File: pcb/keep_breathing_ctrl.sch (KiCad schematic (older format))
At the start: 5 parts, among them P1 CONN_RASPBERRY

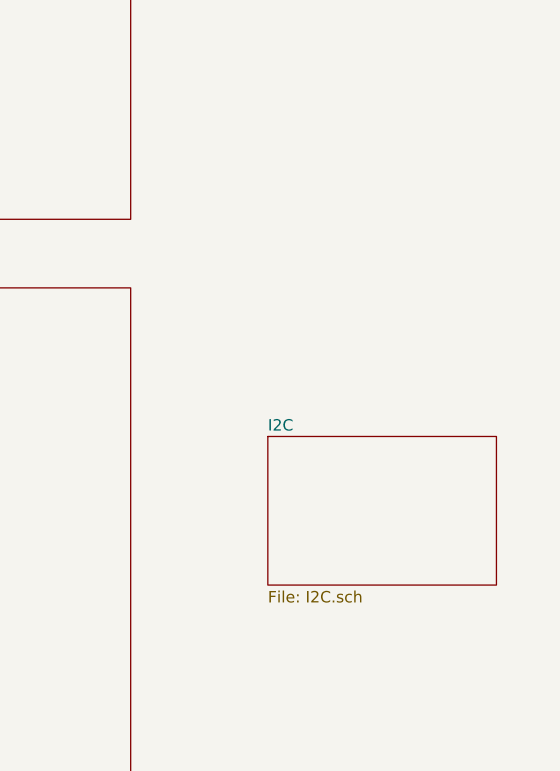
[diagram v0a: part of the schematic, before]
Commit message: RTC to PCB
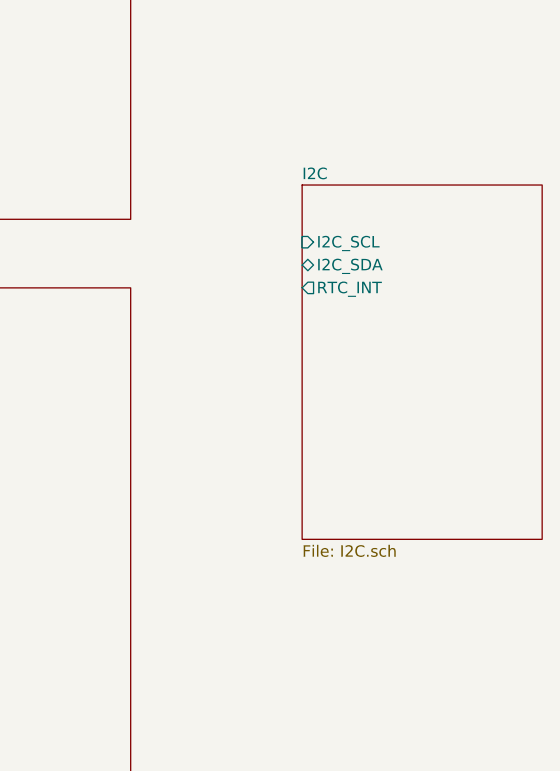
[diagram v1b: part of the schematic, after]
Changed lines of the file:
@@
 $EndSheet
 $Sheet
-S 8550 3150 1000 650
+S 8700 2050 1050 1550
 U 5E8F4152
 F0 "I2C" 50
 F1 "I2C.sch" 50
+F2 "I2C_SDA" B L 8700 2400 50
+F3 "I2C_SCL" I L 8700 2300 50
+F4 "RTC_INT" O L 8700 2500 50
 $EndSheet
 $EndSCHEMATC

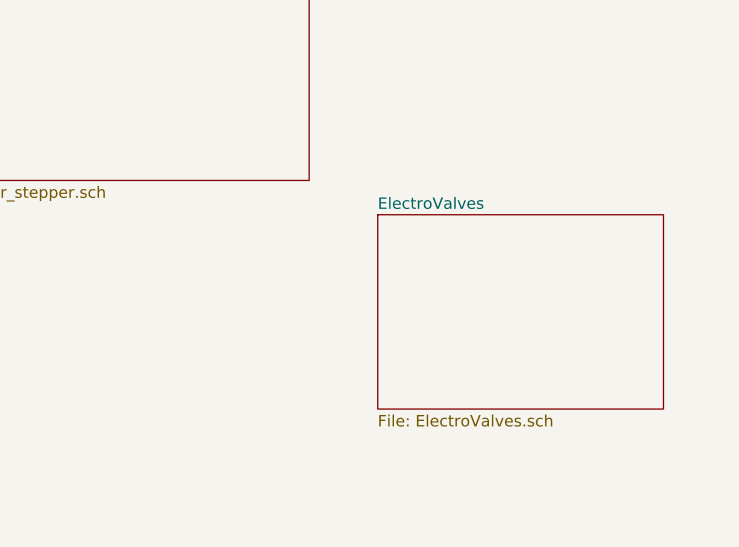
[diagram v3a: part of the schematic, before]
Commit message: connecting relays to the i2c-gpios
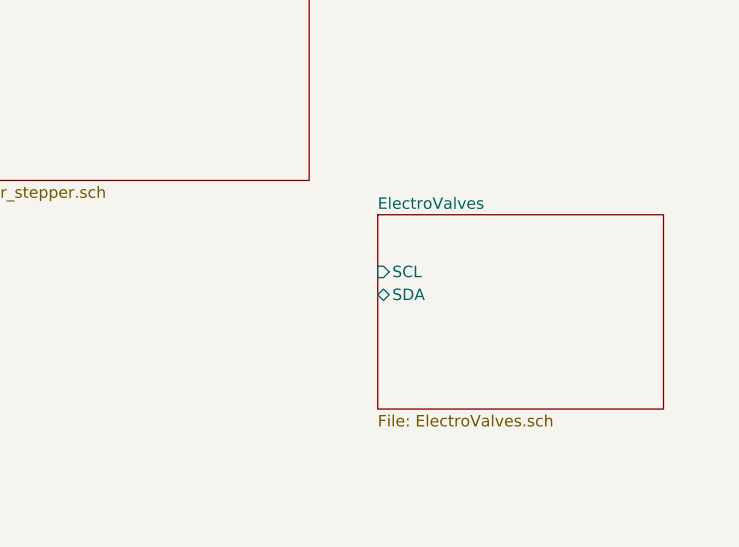
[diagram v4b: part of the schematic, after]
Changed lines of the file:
@@
 F0 "ElectroValves" 50
 F1 "ElectroValves.sch" 50
+F2 "SCL" I L 8250 5250 50
+F3 "SDA" B L 8250 5350 50
 $EndSheet
 $Comp

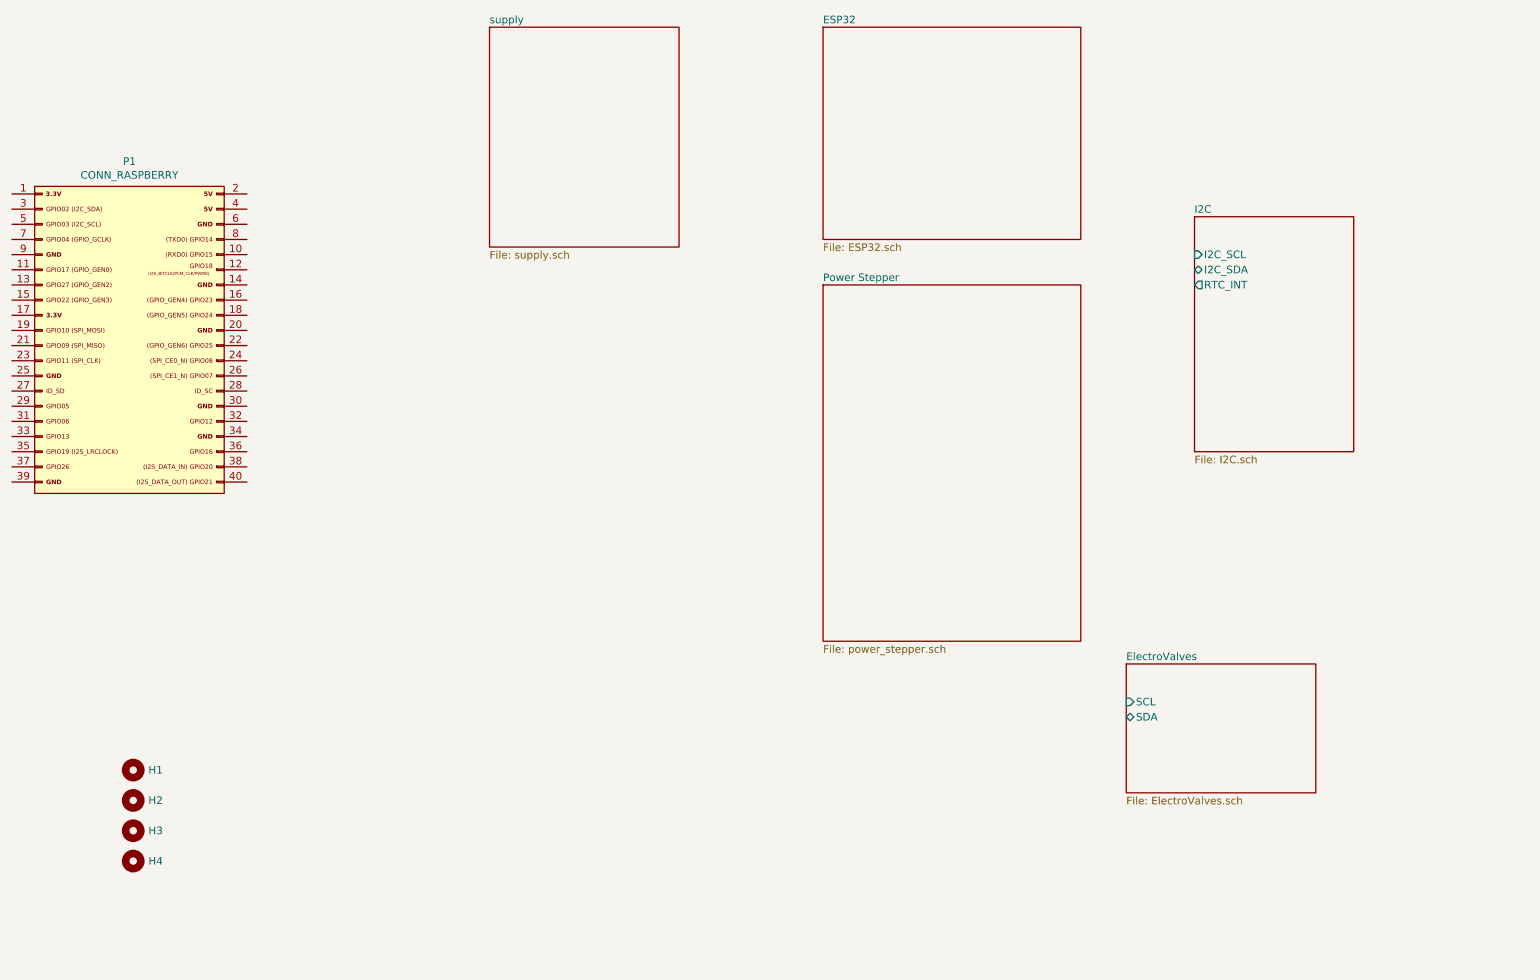
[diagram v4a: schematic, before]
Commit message: connecting esp32 signals
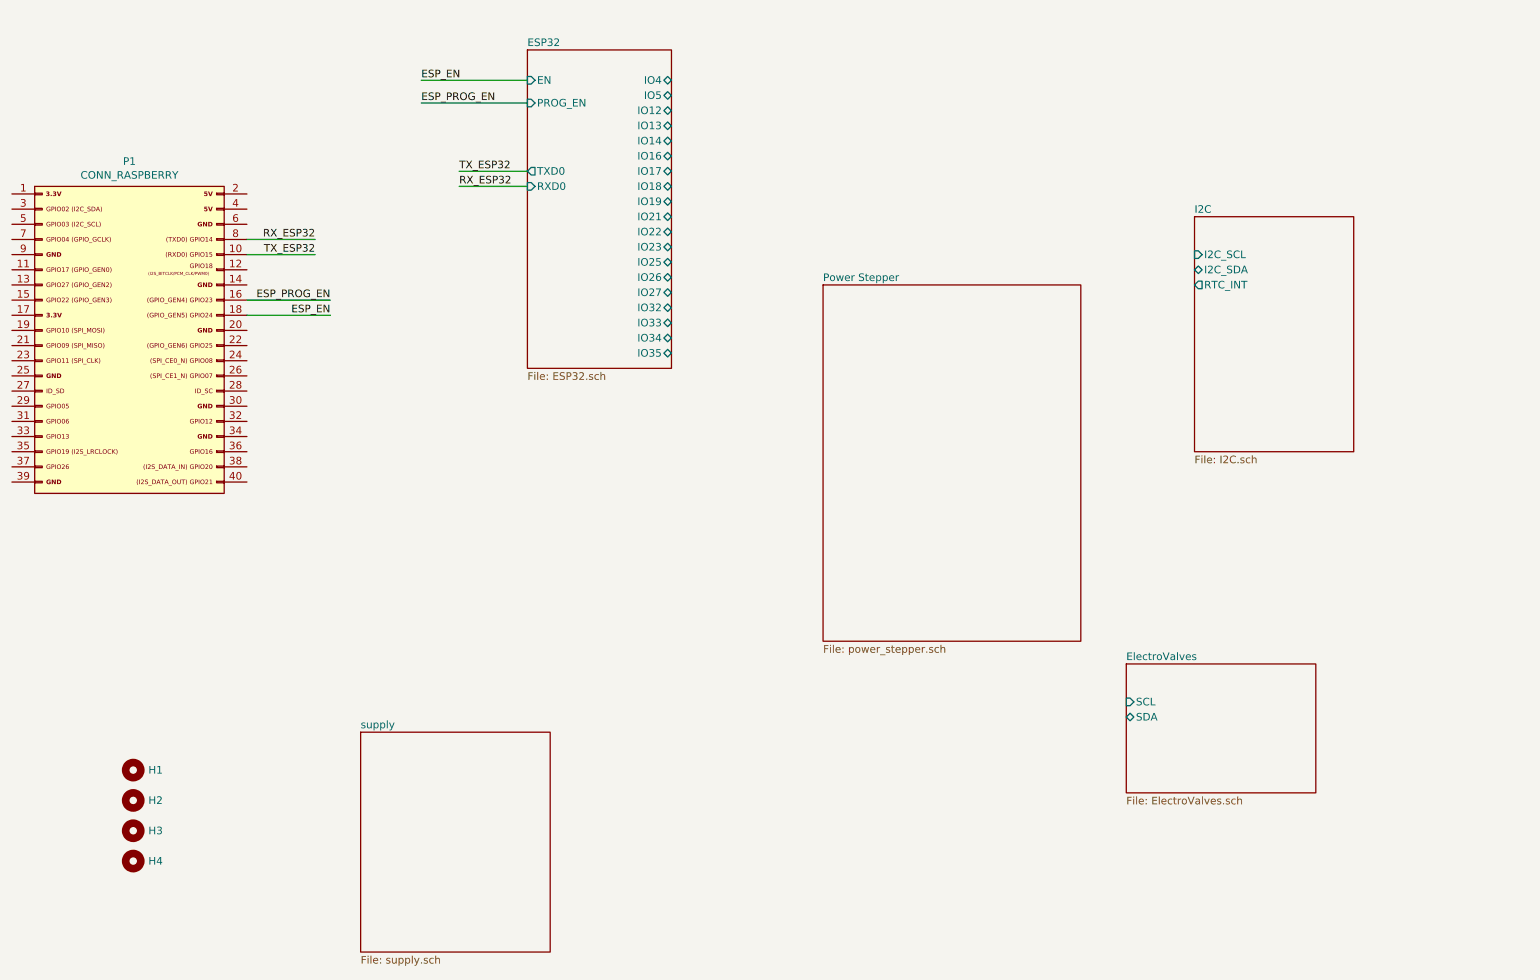
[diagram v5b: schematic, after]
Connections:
- net TX_ESP32: now reaches P1.10 (P10)
- net ESP_PROG_EN: now reaches P1.16 (P16)
- net ESP_EN: now reaches P1.18 (P18)
- net RX_ESP32: now reaches P1.8 (P8)
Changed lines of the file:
@@
 $EndComp
 $Sheet
-S 6250 800  1700 1400
+S 4300 950  950  2100
 U 5E9877D5
 F0 "ESP32" 50
 F1 "ESP32.sch" 50
+F2 "TXD0" O L 4300 1750 50
+F3 "RXD0" I L 4300 1850 50
+F4 "PROG_EN" I L 4300 1300 50
+F5 "IO23" B R 5250 2250 50
+F6 "IO22" B R 5250 2150 50
+F7 "IO19" B R 5250 1950 50
+F8 "IO18" B R 5250 1850 50
+F9 "IO5" B R 5250 1250 50
+F10 "IO17" B R 5250 1750 50
+F11 "IO16" B R 5250 1650 50
+F12 "IO4" B R 5250 1150 50
+F13 "IO12" B R 5250 1350 50
+F14 "IO14" B R 5250 1550 50
+F15 "IO27" B R 5250 2550 50
+F16 "IO26" B R 5250 2450 50
+F17 "IO25" B R 5250 2350 50
+F18 "IO33" B R 5250 2750 50
+F19 "IO32" B R 5250 2650 50
+F20 "IO35" B R 5250 2950 50
+F21 "IO34" B R 5250 2850 50
+F22 "IO13" B R 5250 1450 50
+F23 "IO21" B R 5250 2050 50
+F24 "EN" I L 4300 1150 50
 $EndSheet
 $Sheet
@@
 $EndComp
 $Sheet
-S 4050 800  1250 1450
+S 3200 5450 1250 1450
 U 5E8E60A3
 F0 "supply" 50
@@
 F4 "RTC_INT" O L 8700 2500 50
 $EndSheet
+Wire Wire Line
+	4300 1750 3850 1750
+Wire Wire Line
+	3850 1850 4300 1850
+Text Label 3850 1750 0    50   ~ 0
+TX_ESP32
+Text Label 3850 1850 0    50   ~ 0
+RX_ESP32
+Wire Wire Line
+	2450 2300 2900 2300
+Wire Wire Line
+	2900 2200 2450 2200
+Text Label 2900 2300 2    50   ~ 0
+TX_ESP32
+Text Label 2900 2200 2    50   ~ 0
+RX_ESP32
+Text Label 3600 1300 0    50   ~ 0
+ESP_PROG_EN
+Wire Wire Line
+	4300 1150 3600 1150
+Wire Wire Line
+	4300 1300 3600 1300
+Text Label 3600 1150 0    50   ~ 0
+ESP_EN
+Text Label 3000 2600 2    50   ~ 0
+ESP_PROG_EN
+Wire Wire Line
+	2450 2700 3000 2700
+Wire Wire Line
+	2450 2600 3000 2600
+Text Label 3000 2700 2    50   ~ 0
+ESP_EN
 $EndSCHEMATC

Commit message: added connections to ElectroValves sheet
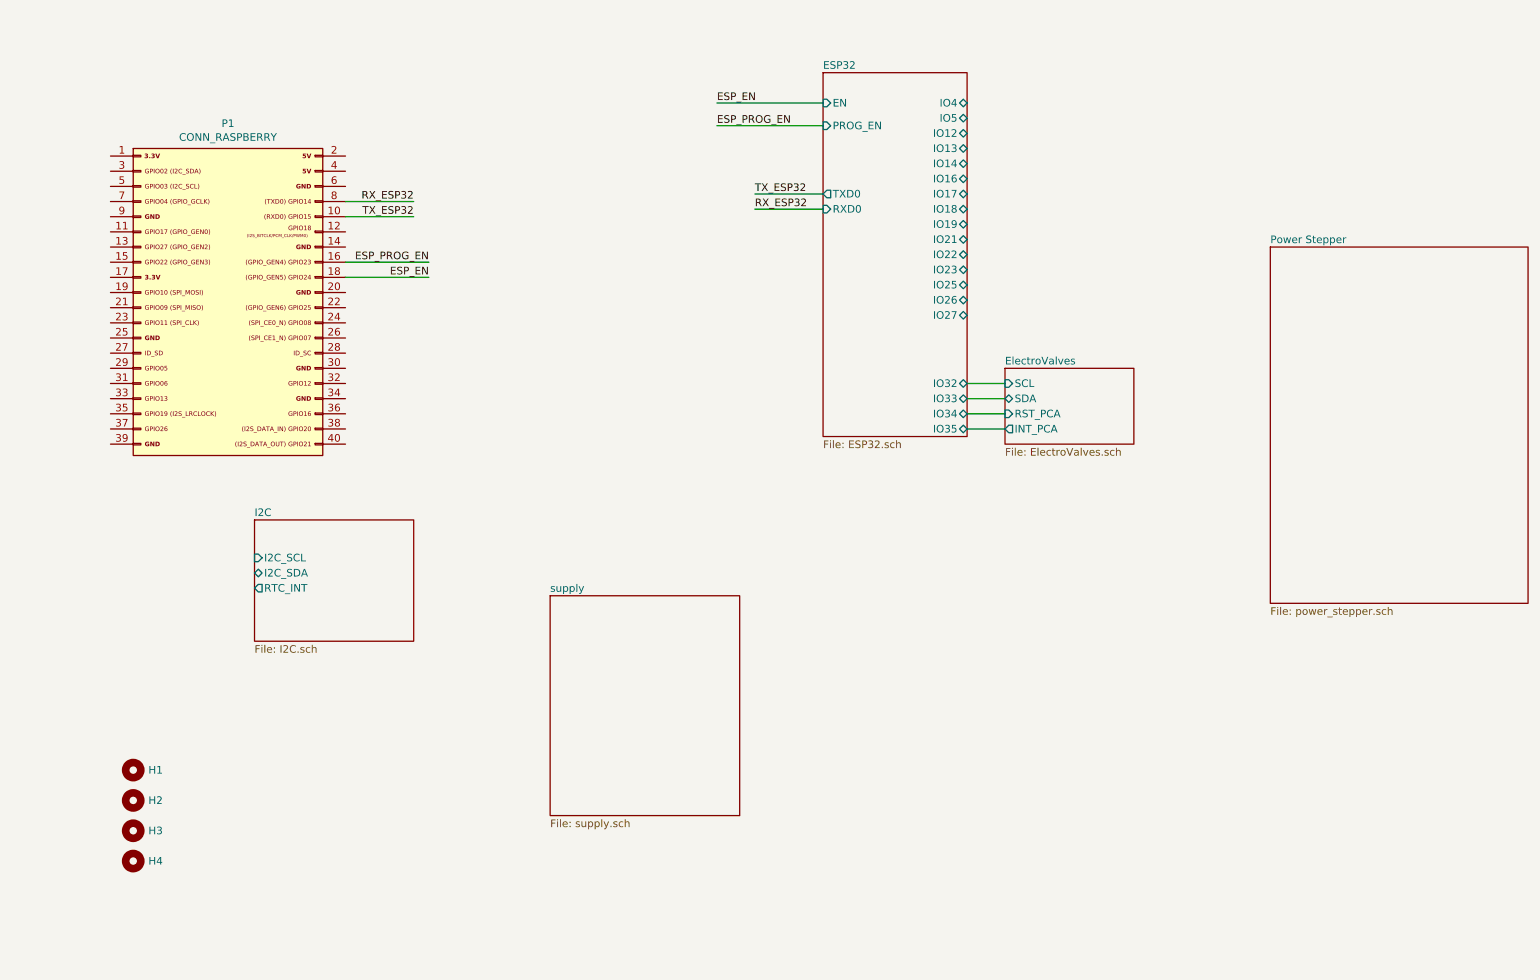
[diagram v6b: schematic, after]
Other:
- moved on the sheet: P1
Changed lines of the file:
@@
 EESchema Schematic File Version 4
 LIBS:keep_breathing_ctrl-cache
-EELAYER 30 0
+EELAYER 26 0
 EELAYER END
 $Descr A4 11693 8268
@@
 $EndDescr
 $Sheet
-S 6250 2500 1700 2350
+S 9200 2250 1700 2350
 U 5E968E64
 F0 "Power Stepper" 50
@@
 L conn_raspberry_2x40:CONN_RASPBERRY P1
 U 1 1 5E9821B0
-P 1950 2850
-F 0 "P1" H 1675 4015 50  0000 C CNN
-F 1 "CONN_RASPBERRY" H 1675 3924 50  0000 C CNN
-F 2 "TH:RPI_MATRIX_40" H 1675 3931 60  0001 C CNN
-F 3 "" H 1150 1900 60  0000 C CNN
-	1    1950 2850
+P 2600 2600
+F 0 "P1" H 2325 3765 50  0000 C CNN
+F 1 "CONN_RASPBERRY" H 2325 3674 50  0000 C CNN
+F 2 "TH:RPI_MATRIX_40" H 2325 3681 60  0001 C CNN
+F 3 "" H 1800 1650 60  0000 C CNN
+	1    2600 2600
 	1    0    0    -1
 $EndComp
 $Sheet
-S 4300 950  950  2100
+S 6250 1100 950  2400
 U 5E9877D5
 F0 "ESP32" 50
 F1 "ESP32.sch" 50
-F2 "TXD0" O L 4300 1750 50
-F3 "RXD0" I L 4300 1850 50
-F4 "PROG_EN" I L 4300 1300 50
-F5 "IO23" B R 5250 2250 50
-F6 "IO22" B R 5250 2150 50
-F7 "IO19" B R 5250 1950 50
-F8 "IO18" B R 5250 1850 50
-F9 "IO5" B R 5250 1250 50
-F10 "IO17" B R 5250 1750 50
-F11 "IO16" B R 5250 1650 50
-F12 "IO4" B R 5250 1150 50
-F13 "IO12" B R 5250 1350 50
-F14 "IO14" B R 5250 1550 50
-F15 "IO27" B R 5250 2550 50
-F16 "IO26" B R 5250 2450 50
-F17 "IO25" B R 5250 2350 50
-F18 "IO33" B R 5250 2750 50
-F19 "IO32" B R 5250 2650 50
-F20 "IO35" B R 5250 2950 50
-F21 "IO34" B R 5250 2850 50
-F22 "IO13" B R 5250 1450 50
-F23 "IO21" B R 5250 2050 50
-F24 "EN" I L 4300 1150 50
+F2 "TXD0" O L 6250 1900 50
+F3 "RXD0" I L 6250 2000 50
+F4 "PROG_EN" I L 6250 1450 50
+F5 "IO23" B R 7200 2400 50
+F6 "IO22" B R 7200 2300 50
+F7 "IO19" B R 7200 2100 50
+F8 "IO18" B R 7200 2000 50
+F9 "IO5" B R 7200 1400 50
+F10 "IO17" B R 7200 1900 50
+F11 "IO16" B R 7200 1800 50
+F12 "IO4" B R 7200 1300 50
+F13 "IO12" B R 7200 1500 50
+F14 "IO14" B R 7200 1700 50
+F15 "IO27" B R 7200 2700 50
+F16 "IO26" B R 7200 2600 50
+F17 "IO25" B R 7200 2500 50
+F18 "IO33" B R 7200 3250 50
+F19 "IO32" B R 7200 3150 50
+F20 "IO35" B R 7200 3450 50
+F21 "IO34" B R 7200 3350 50
+F22 "IO13" B R 7200 1600 50
+F23 "IO21" B R 7200 2200 50
+F24 "EN" I L 6250 1300 50
 $EndSheet
 $Sheet
-S 8250 5000 1250 850
+S 7450 3050 850  500
 U 5E99077D
 F0 "ElectroValves" 50
 F1 "ElectroValves.sch" 50
-F2 "SCL" I L 8250 5250 50
-F3 "SDA" B L 8250 5350 50
+F2 "SCL" I L 7450 3150 50
+F3 "SDA" B L 7450 3250 50
+F4 "RST_PCA" I L 7450 3350 50
+F5 "INT_PCA" O L 7450 3450 50
 $EndSheet
 $Comp
@@
 $EndComp
 $Sheet
-S 3200 5450 1250 1450
+S 4450 4550 1250 1450
 U 5E8E60A3
 F0 "supply" 50
@@
 $EndSheet
 $Sheet
-S 8700 2050 1050 1550
+S 2500 4050 1050 800
 U 5E8F4152
 F0 "I2C" 50
 F1 "I2C.sch" 50
-F2 "I2C_SDA" B L 8700 2400 50
-F3 "I2C_SCL" I L 8700 2300 50
-F4 "RTC_INT" O L 8700 2500 50
+F2 "I2C_SDA" B L 2500 4400 50
+F3 "I2C_SCL" I L 2500 4300 50
+F4 "RTC_INT" O L 2500 4500 50
 $EndSheet
 Wire Wire Line
-	4300 1750 3850 1750
+	6250 1900 5800 1900
 Wire Wire Line
-	3850 1850 4300 1850
-Text Label 3850 1750 0    50   ~ 0
+	5800 2000 6250 2000
+Text Label 5800 1900 0    50   ~ 0
 TX_ESP32
-Text Label 3850 1850 0    50   ~ 0
+Text Label 5800 2000 0    50   ~ 0
 RX_ESP32
 Wire Wire Line
-	2450 2300 2900 2300
+	3100 2050 3550 2050
 Wire Wire Line
-	2900 2200 2450 2200
-Text Label 2900 2300 2    50   ~ 0
+	3550 1950 3100 1950
+Text Label 3550 2050 2    50   ~ 0
 TX_ESP32
-Text Label 2900 2200 2    50   ~ 0
+Text Label 3550 1950 2    50   ~ 0
 RX_ESP32
-Text Label 3600 1300 0    50   ~ 0
+Text Label 5550 1450 0    50   ~ 0
 ESP_PROG_EN
 Wire Wire Line
-	4300 1150 3600 1150
+	6250 1300 5550 1300
 Wire Wire Line
-	4300 1300 3600 1300
-Text Label 3600 1150 0    50   ~ 0
+	6250 1450 5550 1450
+Text Label 5550 1300 0    50   ~ 0
 ESP_EN
-Text Label 3000 2600 2    50   ~ 0
+Text Label 3650 2350 2    50   ~ 0
 ESP_PROG_EN
 Wire Wire Line
-	2450 2700 3000 2700
+	3100 2450 3650 2450
 Wire Wire Line
-	2450 2600 3000 2600
-Text Label 3000 2700 2    50   ~ 0
+	3100 2350 3650 2350
+Text Label 3650 2450 2    50   ~ 0
 ESP_EN
+Wire Wire Line
+	7200 3150 7450 3150
+Wire Wire Line
+	7200 3250 7450 3250
+Wire Wire Line
+	7200 3350 7450 3350
+Wire Wire Line
+	7200 3450 7450 3450
 $EndSCHEMATC
